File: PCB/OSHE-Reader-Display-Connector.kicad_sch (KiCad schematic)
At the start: 18 parts, among them J3 Conn_01x24_MountingPin, Q1 Si1308EDL

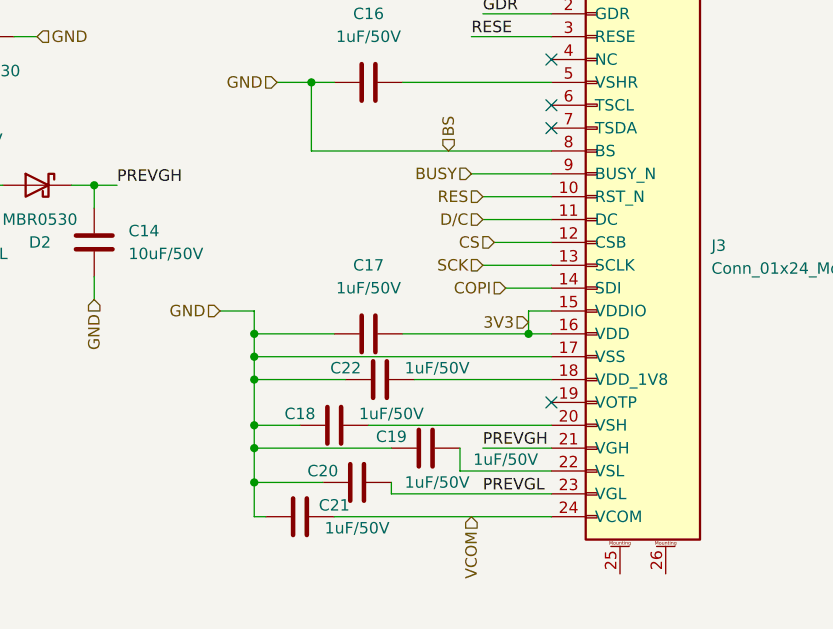
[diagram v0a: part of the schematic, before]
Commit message: updated sd card main sheet pins, swapped big caps for small ones on display connector for better readability
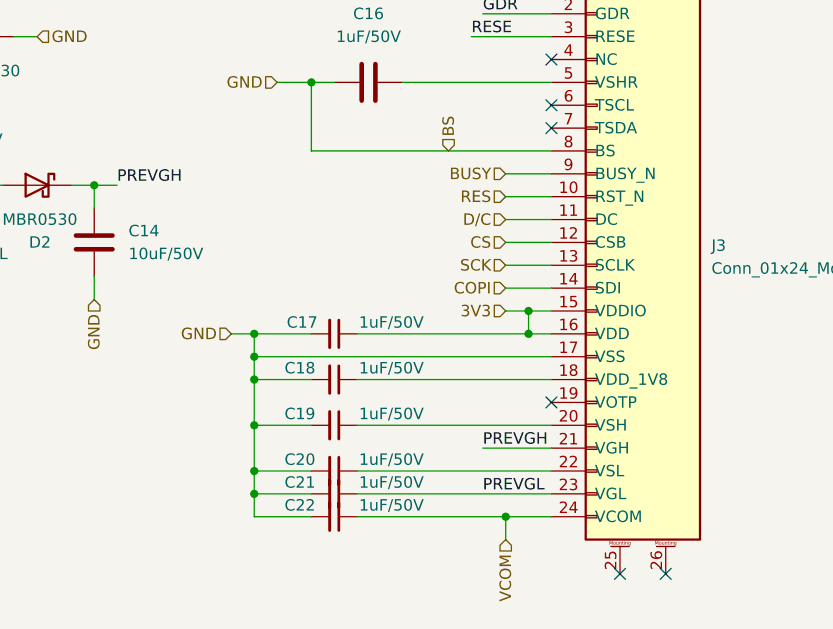
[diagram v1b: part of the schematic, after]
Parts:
- C17: symbol Device:C -> Device:C_Small
- C18: renamed from C22; symbol Device:C -> Device:C_Small
- C19: renamed from C18; symbol Device:C -> Device:C_Small
- C20: renamed from C19; symbol Device:C -> Device:C_Small
- C21: renamed from C20; symbol Device:C -> Device:C_Small
- C22: renamed from C21; symbol Device:C -> Device:C_Small
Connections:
- no-connect marks 5 -> 7
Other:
- moved on the sheet: C17, C18, C20, C21, C22

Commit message: HOPEFULLY GOOD FOR EVER (good for first semester) :)
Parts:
- renumbered C13 to C14, C14 to C15, C12 to C16, C16 to C17, C17 to C18, C18 to C19, C19 to C20, C20 to C21, C21 to C22, C22 to C23, Q1 to Q2
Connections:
- net BS renamed GND
- net RES renamed RESET
- net VCOM: no longer names the net of C23.1, J3.24 (VCOM)
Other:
- moved on the sheet: C14, C17, C18, C19, C20, C21, C22, C23, J3, L2

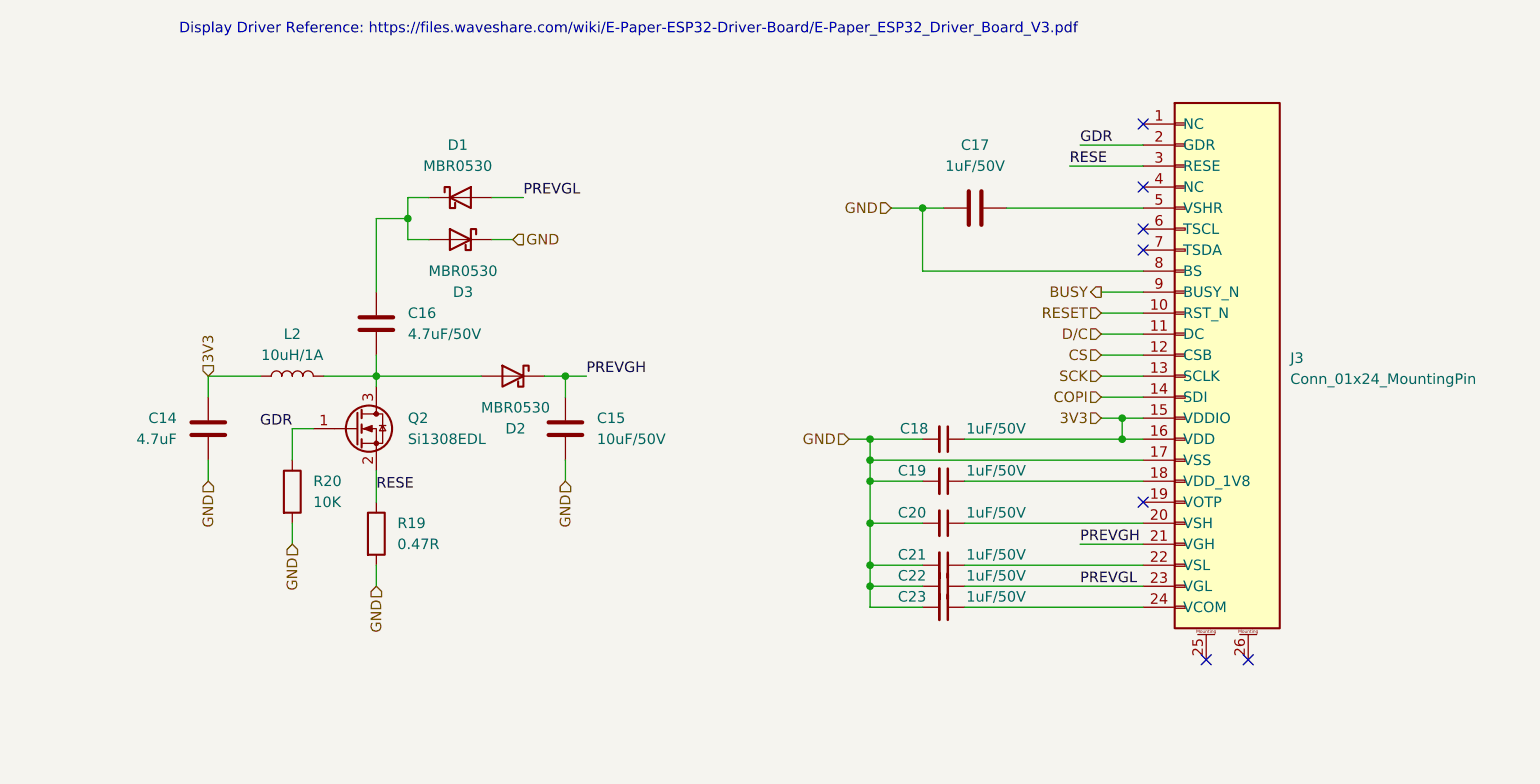
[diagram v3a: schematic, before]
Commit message: Footprints added
All footprints added (problem with J1 for some reason) ((pads of the display driver))
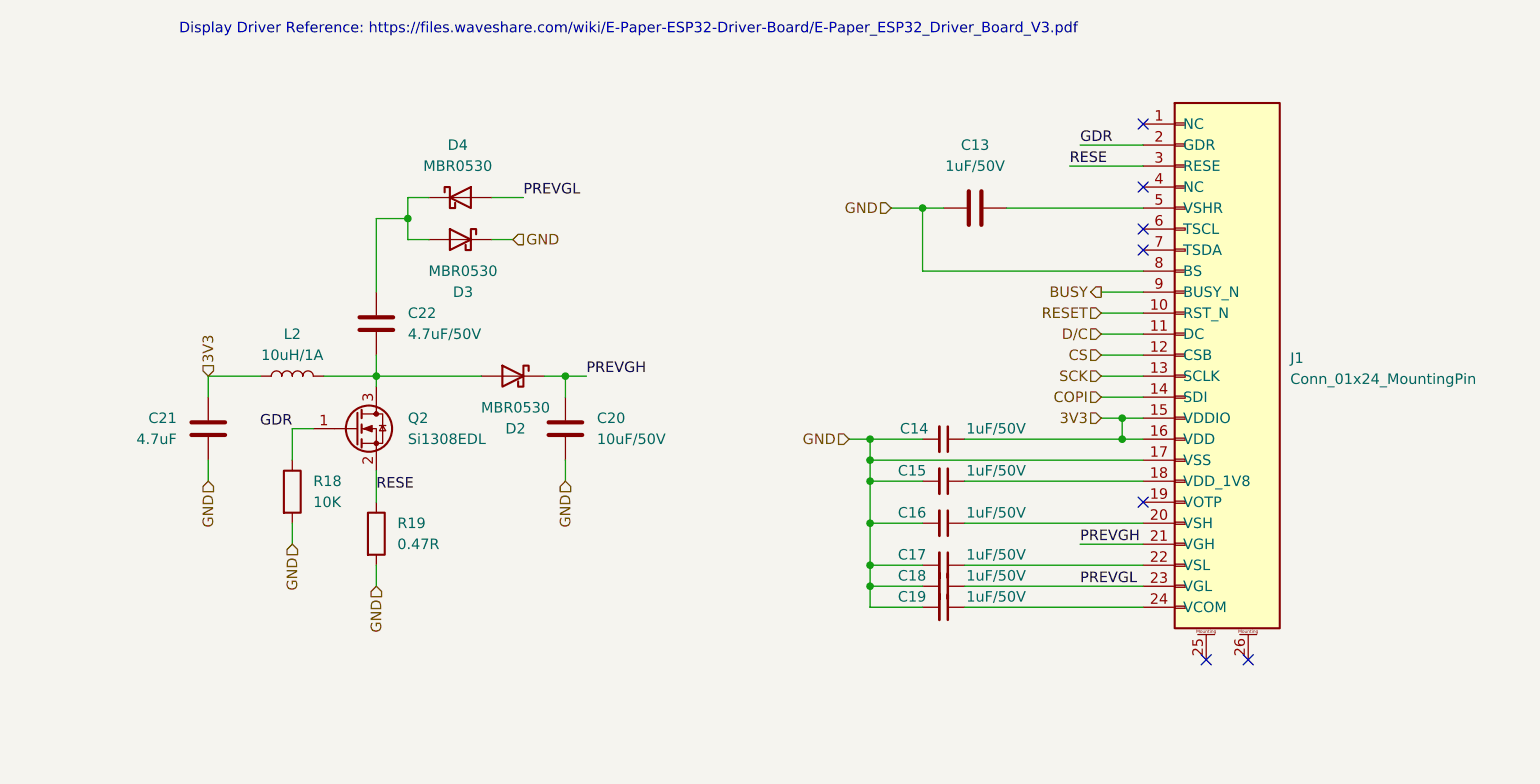
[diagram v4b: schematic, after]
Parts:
- C13: renamed from C17; footprint (none) -> Capacitor_SMD:C_1206_3216Metric
- C14: renamed from C18; footprint (none) -> Capacitor_SMD:C_1206_3216Metric
- C15: renamed from C19; footprint (none) -> Capacitor_SMD:C_1206_3216Metric
- C16: renamed from C20; footprint (none) -> Capacitor_SMD:C_1206_3216Metric
- C17: renamed from C21; footprint (none) -> Capacitor_SMD:C_1206_3216Metric
- C18: renamed from C22; footprint (none) -> Capacitor_SMD:C_1206_3216Metric
- C19: renamed from C23; footprint (none) -> Capacitor_SMD:C_1206_3216Metric
- C20: renamed from C15; footprint (none) -> Capacitor_SMD:C_1206_3216Metric
- C21: renamed from C14; footprint (none) -> Capacitor_SMD:C_1206_3216Metric
- C22: renamed from C16; footprint (none) -> Capacitor_SMD:C_1206_3216Metric
- L2: footprint (none) -> Inductor_SMD:L_1812_4532Metric
- R18: renamed from R20; footprint (none) -> Resistor_SMD:R_1206_3216Metric
- R19: footprint (none) -> Resistor_SMD:R_1206_3216Metric
- renumbered D1 to D4, J3 to J1
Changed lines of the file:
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@@
 		(on_board yes)
 		(dnp no)
-		(property "Reference" "C20"
+		(property "Reference" "C16"
 			(at 113.03 76.2 90)
 			(effects
@@
 			)
 		)
-		(property "Footprint" ""
+		(property "Footprint" "Capacitor_SMD:C_1206_3216Metric"
 			(at 116.84 77.47 0)
 			(effects
@@
 		)
 		(instances
+			(project "OSHE-Reader-Display-Connector"
+				(path "/2df8b7b4-9a23-4c1b-b49e-cc00a8453b9c"
+					(reference "C16")
+					(unit 1)
+				)
+			)
 			(project "OSHE-Reader-PCB"
 				(path "/3f072c92-e35a-4654-839b-728bd3dc3a46/ab4c386c-ccef-4fd2-9471-e05e7dab2219"
@@
 		(dnp no)
 		(fields_autoplaced yes)
-		(property "Reference" "J3"
+		(property "Reference" "J1"
 			(at 158.75 57.5055 0)
 			(effects
@@
 		)
 		(instances
+			(project "OSHE-Reader-Display-Connector"
+				(path "/2df8b7b4-9a23-4c1b-b49e-cc00a8453b9c"
+					(reference "J1")
+					(unit 1)
+				)
+			)
 			(project "OSHE-Reader-PCB"
 				(path "/3f072c92-e35a-4654-839b-728bd3dc3a46/ab4c386c-ccef-4fd2-9471-e05e7dab2219"
@@
 		(dnp no)
 		(fields_autoplaced yes)
-		(property "Reference" "R20"
+		(property "Reference" "R18"
 			(at 40.64 72.3899 0)
 			(effects
@@
 			)
 		)
-		(property "Footprint" ""
+		(property "Footprint" "Resistor_SMD:R_1206_3216Metric"
 			(at 36.322 73.66 90)
 			(effects
@@
 		)
 		(instances
+			(project "OSHE-Reader-Display-Connector"
+				(path "/2df8b7b4-9a23-4c1b-b49e-cc00a8453b9c"
+					(reference "R18")
+					(unit 1)
+				)
+			)
 			(project "OSHE-Reader-PCB"
 				(path "/3f072c92-e35a-4654-839b-728bd3dc3a46/ab4c386c-ccef-4fd2-9471-e05e7dab2219"
@@
 		)
 		(instances
+			(project "OSHE-Reader-Display-Connector"
+				(path "/2df8b7b4-9a23-4c1b-b49e-cc00a8453b9c"
+					(reference "Q2")
+					(unit 1)
+				)
+			)
 			(project "OSHE-Reader-PCB"
 				(path "/3f072c92-e35a-4654-839b-728bd3dc3a46/ab4c386c-ccef-4fd2-9471-e05e7dab2219"
@@
 		(dnp no)
 		(fields_autoplaced yes)
-		(property "Reference" "D1"
+		(property "Reference" "D4"
 			(at 58.1025 31.75 0)
 			(effects
@@
 		)
 		(instances
+			(project "OSHE-Reader-Display-Connector"
+				(path "/2df8b7b4-9a23-4c1b-b49e-cc00a8453b9c"
+					(reference "D4")
+					(unit 1)
+				)
+			)
 			(project "OSHE-Reader-PCB"
 				(path "/3f072c92-e35a-4654-839b-728bd3dc3a46/ab4c386c-ccef-4fd2-9471-e05e7dab2219"
@@
 		(on_board yes)
 		(dnp no)
-		(property "Reference" "C23"
+		(property "Reference" "C19"
 			(at 113.03 86.36 90)
 			(effects
@@
 			)
 		)
-		(property "Footprint" ""
+		(property "Footprint" "Capacitor_SMD:C_1206_3216Metric"
 			(at 116.84 87.63 0)
 			(effects
@@
 		)
 		(instances
+			(project "OSHE-Reader-Display-Connector"
+				(path "/2df8b7b4-9a23-4c1b-b49e-cc00a8453b9c"
+					(reference "C19")
+					(unit 1)
+				)
+			)
 			(project "OSHE-Reader-PCB"
 				(path "/3f072c92-e35a-4654-839b-728bd3dc3a46/ab4c386c-ccef-4fd2-9471-e05e7dab2219"
@@
 		(on_board yes)
 		(dnp no)
-		(property "Reference" "C21"
+		(property "Reference" "C17"
 			(at 113.03 81.28 90)
 			(effects
@@
 			)
 		)
-		(property "Footprint" ""
+		(property "Footprint" "Capacitor_SMD:C_1206_3216Metric"
 			(at 116.84 82.55 0)
 			(effects
@@
 		)
 		(instances
+			(project "OSHE-Reader-Display-Connector"
+				(path "/2df8b7b4-9a23-4c1b-b49e-cc00a8453b9c"
+					(reference "C17")
+					(unit 1)
+				)
+			)
 			(project "OSHE-Reader-PCB"
 				(path "/3f072c92-e35a-4654-839b-728bd3dc3a46/ab4c386c-ccef-4fd2-9471-e05e7dab2219"
@@
 			)
 		)
-		(property "Footprint" ""
+		(property "Footprint" "Resistor_SMD:R_1206_3216Metric"
 			(at 46.482 78.74 90)
 			(effects
@@
 		)
 		(instances
+			(project "OSHE-Reader-Display-Connector"
+				(path "/2df8b7b4-9a23-4c1b-b49e-cc00a8453b9c"
+					(reference "R19")
+					(unit 1)
+				)
+			)
 			(project "OSHE-Reader-PCB"
 				(path "/3f072c92-e35a-4654-839b-728bd3dc3a46/ab4c386c-ccef-4fd2-9471-e05e7dab2219"
@@
 		(on_board yes)
 		(dnp no)
-		(property "Reference" "C18"
+		(property "Reference" "C14"
 			(at 113.2776 66.04 90)
 			(effects
@@
 			)
 		)
-		(property "Footprint" ""
+		(property "Footprint" "Capacitor_SMD:C_1206_3216Metric"
 			(at 116.84 67.31 0)
 			(effects
@@
 		)
 		(instances
+			(project "OSHE-Reader-Display-Connector"
+				(path "/2df8b7b4-9a23-4c1b-b49e-cc00a8453b9c"
+					(reference "C14")
+					(unit 1)
+				)
+			)
 			(project "OSHE-Reader-PCB"
 				(path "/3f072c92-e35a-4654-839b-728bd3dc3a46/ab4c386c-ccef-4fd2-9471-e05e7dab2219"
@@
 		(dnp no)
 		(fields_autoplaced yes)
-		(property "Reference" "C17"
+		(property "Reference" "C13"
 			(at 120.65 31.75 90)
 			(effects
@@
 			)
 		)
-		(property "Footprint" ""
+		(property "Footprint" "Capacitor_SMD:C_1206_3216Metric"
 			(at 116.84 40.3352 0)
 			(effects
@@
 		)
 		(instances
+			(project "OSHE-Reader-Display-Connector"
+				(path "/2df8b7b4-9a23-4c1b-b49e-cc00a8453b9c"
+					(reference "C13")
+					(unit 1)
+				)
+			)
 			(project "OSHE-Reader-PCB"
 				(path "/3f072c92-e35a-4654-839b-728bd3dc3a46/ab4c386c-ccef-4fd2-9471-e05e7dab2219"
@@
 		)
 		(instances
+			(project "OSHE-Reader-Display-Connector"
+				(path "/2df8b7b4-9a23-4c1b-b49e-cc00a8453b9c"
+					(reference "D2")
+					(unit 1)
+				)
+			)
 			(project "OSHE-Reader-PCB"
 				(path "/3f072c92-e35a-4654-839b-728bd3dc3a46/ab4c386c-ccef-4fd2-9471-e05e7dab2219"
@@
 		)
 		(instances
+			(project "OSHE-Reader-Display-Connector"
+				(path "/2df8b7b4-9a23-4c1b-b49e-cc00a8453b9c"
+					(reference "D3")
+					(unit 1)
+				)
+			)
 			(project "OSHE-Reader-PCB"
 				(path "/3f072c92-e35a-4654-839b-728bd3dc3a46/ab4c386c-ccef-4fd2-9471-e05e7dab2219"
@@
 		(on_board yes)
 		(dnp no)
-		(property "Reference" "C22"
+		(property "Reference" "C18"
 			(at 113.03 83.82 90)
 			(effects
@@
 			)
 		)
-		(property "Footprint" ""
+		(property "Footprint" "Capacitor_SMD:C_1206_3216Metric"
 			(at 116.84 85.09 0)
 			(effects
@@
 		)
 		(instances
+			(project "OSHE-Reader-Display-Connector"
+				(path "/2df8b7b4-9a23-4c1b-b49e-cc00a8453b9c"
+					(reference "C18")
+					(unit 1)
+				)
+			)
 			(project "OSHE-Reader-PCB"
 				(path "/3f072c92-e35a-4654-839b-728bd3dc3a46/ab4c386c-ccef-4fd2-9471-e05e7dab2219"
@@
 		(on_board yes)
 		(dnp no)
-		(property "Reference" "C16"
+		(property "Reference" "C22"
 			(at 52.07 52.0699 0)
 			(effects
@@
 			)
 		)
-		(property "Footprint" ""
+		(property "Footprint" "Capacitor_SMD:C_1206_3216Metric"
 			(at 49.2252 57.15 0)
 			(effects
@@
 		)
 		(instances
+			(project "OSHE-Reader-Display-Connector"
+				(path "/2df8b7b4-9a23-4c1b-b49e-cc00a8453b9c"
+					(reference "C22")
+					(unit 1)
+				)
+			)
 			(project "OSHE-Reader-PCB"
 				(path "/3f072c92-e35a-4654-839b-728bd3dc3a46/ab4c386c-ccef-4fd2-9471-e05e7dab2219"
@@
 		(on_board yes)
 		(dnp no)
-		(property "Reference" "C15"
+		(property "Reference" "C20"
 			(at 74.93 64.7699 0)
 			(effects
@@
 			)
 		)
-		(property "Footprint" ""
+		(property "Footprint" "Capacitor_SMD:C_1206_3216Metric"
 			(at 72.0852 69.85 0)
 			(effects
@@
 		)
 		(instances
+			(project "OSHE-Reader-Display-Connector"
+				(path "/2df8b7b4-9a23-4c1b-b49e-cc00a8453b9c"
+					(reference "C20")
+					(unit 1)
+				)
+			)
 			(project "OSHE-Reader-PCB"
 				(path "/3f072c92-e35a-4654-839b-728bd3dc3a46/ab4c386c-ccef-4fd2-9471-e05e7dab2219"
@@
 		(on_board yes)
 		(dnp no)
-		(property "Reference" "C14"
+		(property "Reference" "C21"
 			(at 24.13 64.7699 0)
 			(effects
@@
 			)
 		)
-		(property "Footprint" ""
+		(property "Footprint" "Capacitor_SMD:C_1206_3216Metric"
 			(at 26.9748 69.85 0)
 			(effects
@@
 		)
 		(instances
+			(project "OSHE-Reader-Display-Connector"
+				(path "/2df8b7b4-9a23-4c1b-b49e-cc00a8453b9c"
+					(reference "C21")
+					(unit 1)
+				)
+			)
 			(project "OSHE-Reader-PCB"
 				(path "/3f072c92-e35a-4654-839b-728bd3dc3a46/ab4c386c-ccef-4fd2-9471-e05e7dab2219"
@@
 			)
 		)
-		(property "Footprint" ""
+		(property "Footprint" "Inductor_SMD:L_1812_4532Metric"
 			(at 38.1 59.69 0)
 			(effects
@@
 		)
 		(instances
+			(project "OSHE-Reader-Display-Connector"
+				(path "/2df8b7b4-9a23-4c1b-b49e-cc00a8453b9c"
+					(reference "L2")
+					(unit 1)
+				)
+			)
 			(project "OSHE-Reader-PCB"
 				(path "/3f072c92-e35a-4654-839b-728bd3dc3a46/ab4c386c-ccef-4fd2-9471-e05e7dab2219"
@@
 		(on_board yes)
 		(dnp no)
-		(property "Reference" "C19"
+		(property "Reference" "C15"
 			(at 113.03 71.12 90)
 			(effects
@@
 			)
 		)
-		(property "Footprint" ""
+		(property "Footprint" "Capacitor_SMD:C_1206_3216Metric"
 			(at 116.84 72.39 0)
 			(effects
@@
 		)
 		(instances
+			(project "OSHE-Reader-Display-Connector"
+				(path "/2df8b7b4-9a23-4c1b-b49e-cc00a8453b9c"
+					(reference "C15")
+					(unit 1)
+				)
+			)
 			(project "OSHE-Reader-PCB"
 				(path "/3f072c92-e35a-4654-839b-728bd3dc3a46/ab4c386c-ccef-4fd2-9471-e05e7dab2219"
@@
 		)
 	)
+	(sheet_instances
+		(path "/"
+			(page "1")
+		)
+	)
+	(embedded_fonts no)
 )

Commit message: Did a bunch of work with final preparations of the schematic for pcb routing
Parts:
- renumbered C21 to C14, C20 to C15, C22 to C16, C13 to C17, C14 to C18, C15 to C19, C16 to C20, C17 to C21, C18 to C22, C19 to C23, D4 to D1, J1 to J3, R18 to R20
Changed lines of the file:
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@@
 		(on_board yes)
 		(dnp no)
-		(property "Reference" "C16"
+		(property "Reference" "C20"
 			(at 113.03 76.2 90)
 			(effects
@@
 		(dnp no)
 		(fields_autoplaced yes)
-		(property "Reference" "J1"
+		(property "Reference" "J3"
 			(at 158.75 57.5055 0)
 			(effects
@@
 		(dnp no)
 		(fields_autoplaced yes)
-		(property "Reference" "R18"
+		(property "Reference" "R20"
 			(at 40.64 72.3899 0)
 			(effects
@@
 		(dnp no)
 		(fields_autoplaced yes)
-		(property "Reference" "D4"
+		(property "Reference" "D1"
 			(at 58.1025 31.75 0)
 			(effects
@@
 		(on_board yes)
 		(dnp no)
-		(property "Reference" "C19"
+		(property "Reference" "C23"
 			(at 113.03 86.36 90)
 			(effects
@@
 		(on_board yes)
 		(dnp no)
-		(property "Reference" "C17"
+		(property "Reference" "C21"
 			(at 113.03 81.28 90)
 			(effects
@@
 		(on_board yes)
 		(dnp no)
-		(property "Reference" "C14"
+		(property "Reference" "C18"
 			(at 113.2776 66.04 90)
 			(effects
@@
 		(dnp no)
 		(fields_autoplaced yes)
-		(property "Reference" "C13"
+		(property "Reference" "C17"
 			(at 120.65 31.75 90)
 			(effects
@@
 		(on_board yes)
 		(dnp no)
-		(property "Reference" "C18"
+		(property "Reference" "C22"
 			(at 113.03 83.82 90)
 			(effects
@@
 		(on_board yes)
 		(dnp no)
-		(property "Reference" "C22"
+		(property "Reference" "C16"
 			(at 52.07 52.0699 0)
 			(effects
@@
 		(on_board yes)
 		(dnp no)
-		(property "Reference" "C20"
+		(property "Reference" "C15"
 			(at 74.93 64.7699 0)
 			(effects
@@
 		(on_board yes)
 		(dnp no)
-		(property "Reference" "C21"
+		(property "Reference" "C14"
 			(at 24.13 64.7699 0)
 			(effects
@@
 		(on_board yes)
 		(dnp no)
-		(property "Reference" "C15"
+		(property "Reference" "C19"
 			(at 113.03 71.12 90)
 			(effects

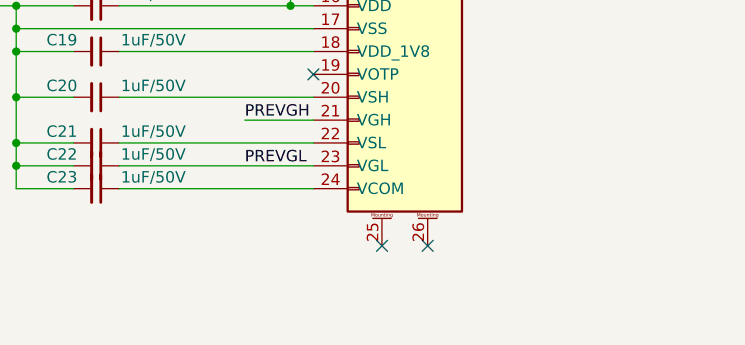
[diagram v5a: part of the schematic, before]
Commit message: Started routing PCB & added case dxf for reference
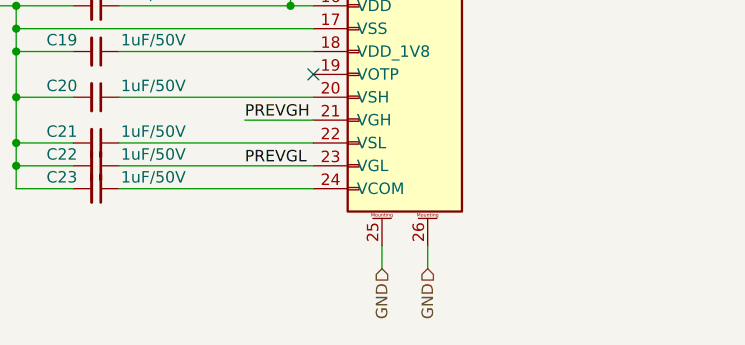
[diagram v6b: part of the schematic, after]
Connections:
- net GND: now also J3.25, J3.26
- no-connect marks 7 -> 5
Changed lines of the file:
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@@
-	)
-	(no_connect
-		(at 148.59 93.98)
-	)
-	(no_connect
-		(at 153.67 93.98)
 	)
 	(no_connect
@@
 	(wire
 		(pts
+			(xy 148.59 93.98) (xy 148.59 96.52)
+		)
+		(stroke
+			(width 0)
+			(type default)
+		)
+	)
+	(wire
+		(pts
 			(xy 48.26 59.69) (xy 60.96 59.69)
 		)
@@
 		(pts
 			(xy 107.95 69.85) (xy 140.97 69.85)
+		)
+		(stroke
+			(width 0)
+			(type default)
+		)
+	)
+	(wire
+		(pts
+			(xy 153.67 93.98) (xy 153.67 96.52)
 		)
 		(stroke
@@
 		)
 	)
+	(hierarchical_label "GND"
+		(shape input)
+		(at 148.59 96.52 270)
+		(effects
+			(font
+				(size 1.27 1.27)
+			)
+			(justify right)
+		)
+	)
 	(hierarchical_label "CS"
 		(shape input)
@@
 		(effects
 			(font
+				(size 1.27 1.27)
+			)
+			(justify right)
+		)
+	)
+	(hierarchical_label "GND"
+		(shape input)
+		(at 153.67 96.52 270)
+		(effects
+			(font
